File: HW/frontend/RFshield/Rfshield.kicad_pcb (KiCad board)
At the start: 4 copper layers, 73 x 50.9 mm, 270 parts, among them P10 TXENABLE, P11 RXENABLE, P12 XTAL2, P13 GCK1, P14 GCK2, P15 SGPIO_CLK, P16 DA0, P17 DA4, P18 DA7, P19 DD0, P2 VAA, P20 DD5, P21 DD9, P22 RSSI, P23 GND, P24 GND, P25 GND, P26 GND, P27 GND, P28 GND, P29 GND, P3 SCL, P30 GND, P31 GND, P32 GND, P33 XCVR_CLKOUT, P37 INTR, P38 CLKIN, P39 CLKOUT, P4 SDA, P5 SSP1_SCK, P6 SSP1_MOSI, P7 SSP1_MISO, P8 CS_XCVR, P9 CS_AD, Q1 MOSFET_P, T1 RX_BALUN, T2 TX_BALUN, U1 MAX2837, U2 MAX5864, U3 SI5351C, X1 GSG-XTAL4PIN

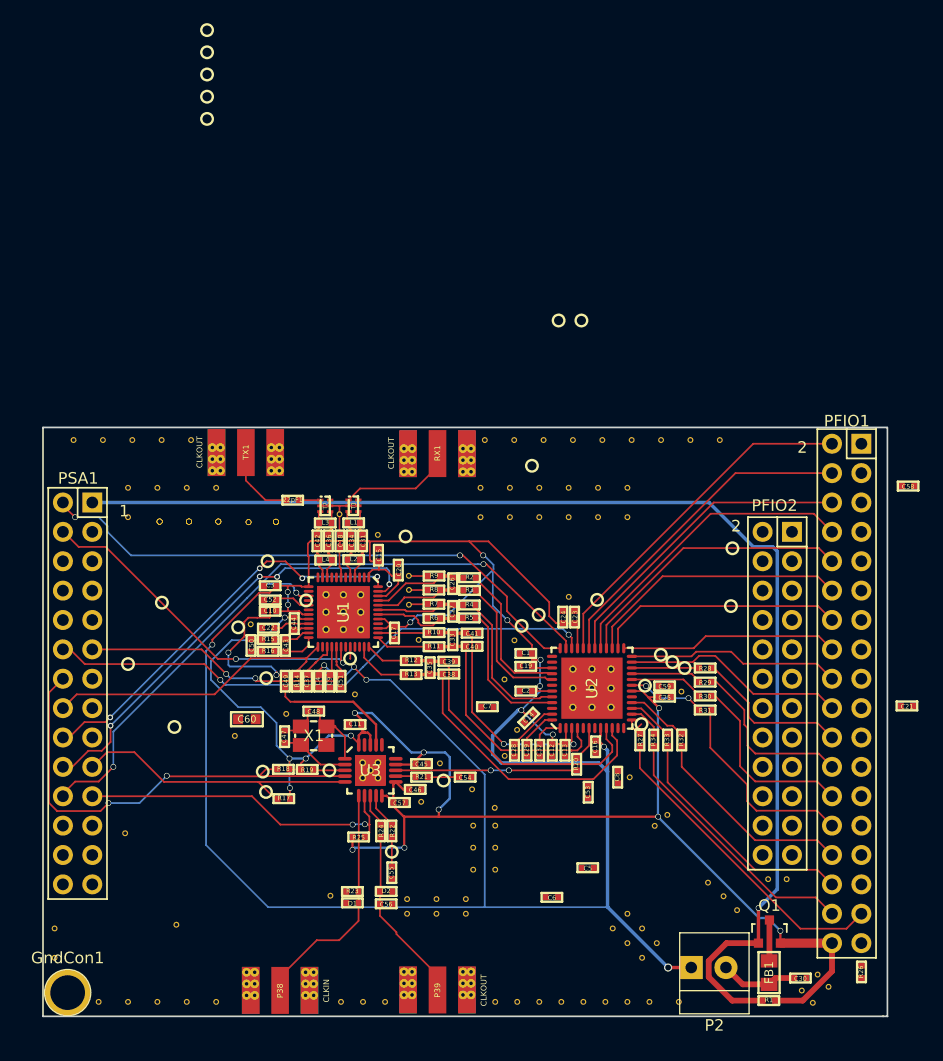
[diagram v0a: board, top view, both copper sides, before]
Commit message: pcb board has been finished
please check my pcb and spot the flaws
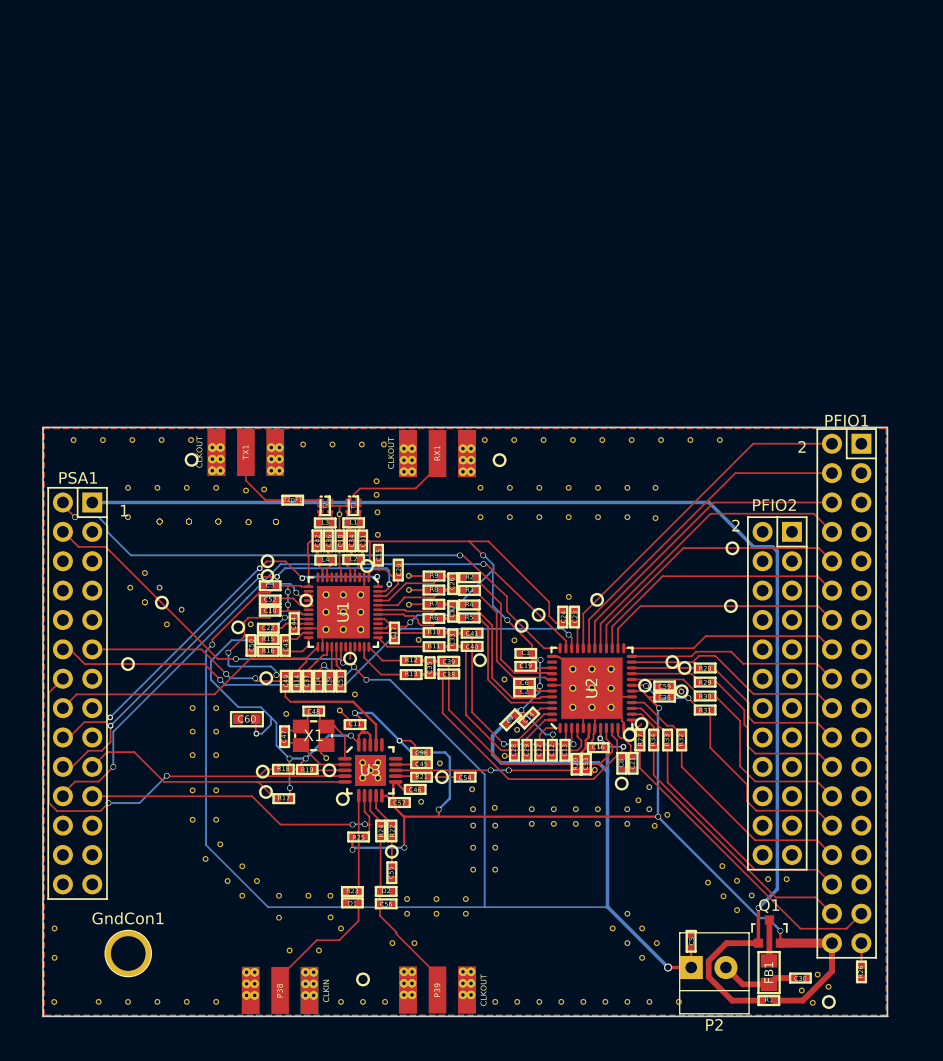
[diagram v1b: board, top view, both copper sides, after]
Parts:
- added TH13: CONN_1, opendous:1Pin_12mil_VIA, F.Cu at (34.3, 100.2)
- added TH13: CONN_1, opendous:1Pin_12mil_VIA, F.Cu at (32.2, 100.2)
- added TH13: CONN_1, opendous:1Pin_12mil_VIA, F.Cu at (34.3, 97.7)
- added TH13: CONN_1, opendous:1Pin_12mil_VIA, F.Cu at (32.2, 97.7)
- added TH13: CONN_1, opendous:1Pin_12mil_VIA, F.Cu at (32.2, 94.6)
- added TH13: CONN_1, opendous:1Pin_12mil_VIA, F.Cu at (34.3, 94.6)
- added TH13: CONN_1, opendous:1Pin_12mil_VIA, F.Cu at (34.3, 92.6)
- added TH13: CONN_1, opendous:1Pin_12mil_VIA, F.Cu at (32.2, 92.6)
- added TH151: CONN_1, opendous:1Pin_12mil_VIA, F.Cu at (72.3, 74.1)
- added TH151: CONN_1, opendous:1Pin_12mil_VIA, F.Cu at (72.3, 71.5)
- added TH18: CONN_1, opendous:1Pin_12mil_VIA, F.Cu at (67.0, 95.9)
- added TH18: CONN_1, opendous:1Pin_12mil_VIA, F.Cu at (42.3, 106.8)
- added TH18: CONN_1, opendous:1Pin_12mil_VIA, F.Cu at (56.5, 99.3)
- added TH18: CONN_1, opendous:1Pin_12mil_VIA, F.Cu at (61.6, 100.6)
- added TH18: CONN_1, opendous:1Pin_12mil_VIA, F.Cu at (61.6, 99.3)
- added TH18: CONN_1, opendous:1Pin_12mil_VIA, F.Cu at (63.5, 100.6)
- added TH18: CONN_1, opendous:1Pin_12mil_VIA, F.Cu at (63.5, 99.3)
- added TH18: CONN_1, opendous:1Pin_12mil_VIA, F.Cu at (65.4, 100.6)
- added TH18: CONN_1, opendous:1Pin_12mil_VIA, F.Cu at (65.4, 99.3)
- added TH18: CONN_1, opendous:1Pin_12mil_VIA, F.Cu at (67.3, 100.6)
- added TH18: CONN_1, opendous:1Pin_12mil_VIA, F.Cu at (69.8, 100.6)
- added TH18: CONN_1, opendous:1Pin_12mil_VIA, F.Cu at (33.4, 103.6)
- added TH18: CONN_1, opendous:1Pin_12mil_VIA, F.Cu at (67.3, 99.3)
- added TH18: CONN_1, opendous:1Pin_12mil_VIA, F.Cu at (69.8, 99.3)
- added TH18: CONN_1, opendous:1Pin_12mil_VIA, F.Cu at (71.7, 97.4)
- added TH18: CONN_1, opendous:1Pin_12mil_VIA, F.Cu at (71.7, 99.3)
- added TH18: CONN_1, opendous:1Pin_12mil_VIA, F.Cu at (78.0, 104.2)
- added TH18: CONN_1, opendous:1Pin_12mil_VIA, F.Cu at (79.3, 105.5)
- added TH18: CONN_1, opendous:1Pin_12mil_VIA, F.Cu at (80.6, 106.8)
- added TH18: CONN_1, opendous:1Pin_12mil_VIA, F.Cu at (34.6, 102.3)
- added TH18: CONN_1, opendous:1Pin_12mil_VIA, F.Cu at (35.3, 105.5)
- added TH18: CONN_1, opendous:1Pin_12mil_VIA, F.Cu at (36.5, 104.2)
- added TH18: CONN_1, opendous:1Pin_12mil_VIA, F.Cu at (36.5, 106.8)
- added TH18: CONN_1, opendous:1Pin_12mil_VIA, F.Cu at (37.8, 105.5)
- added TH18: CONN_1, opendous:1Pin_12mil_VIA, F.Cu at (39.7, 108.7)
- added TH18: CONN_1, opendous:1Pin_12mil_VIA, F.Cu at (39.7, 106.8)
- added TH23: CONN_1, opendous:1Pin_12mil_VIA, F.Cu at (46.9, 67.8)
- added TH23: CONN_1, opendous:1Pin_12mil_VIA, F.Cu at (44.3, 67.8)
- added TH23: CONN_1, opendous:1Pin_12mil_VIA, F.Cu at (41.8, 67.8)
- added TH23: CONN_1, opendous:1Pin_12mil_VIA, F.Cu at (48.8, 67.8)
- added TH23: CONN_1, opendous:1Pin_12mil_VIA, F.Cu at (48.1, 71.0)
- added TH23: CONN_1, opendous:1Pin_12mil_VIA, F.Cu at (48.1, 72.1)
- added TH23: CONN_1, opendous:1Pin_12mil_VIA, F.Cu at (48.2, 73.6)
- added TH25: CONN_1, opendous:1Pin_12mil_VIA, F.Cu at (45.0, 90.8)
- added TH28: CONN_1, opendous:1Pin_12mil_VIA, F.Cu at (30.0, 83.3)
- added TH28 (x2): CONN_1, opendous:1Pin_12mil_VIA, F.Cu at (28.1, 81.4)
- added TH28: CONN_1, opendous:1Pin_12mil_VIA, F.Cu at (31.3, 82.1)
- added TH28: CONN_1, opendous:1Pin_12mil_VIA, F.Cu at (29.4, 80.2)
- added TH28: CONN_1, opendous:1Pin_12mil_VIA, F.Cu at (26.9, 80.2)
- added TH28: CONN_1, opendous:1Pin_12mil_VIA, F.Cu at (28.1, 78.9)
- added TH30: CONN_1, opendous:1Pin_12mil_VIA, F.Cu at (38.4, 71.7)
- added TH30: CONN_1, opendous:1Pin_12mil_VIA, F.Cu at (36.9, 71.8)
- added TH34: CONN_1, opendous:1Pin_12mil_VIA, F.Cu at (45.1, 109.6)
- added TH34: CONN_1, opendous:1Pin_12mil_VIA, F.Cu at (40.6, 111.5)
- added TH34: CONN_1, opendous:1Pin_12mil_VIA, F.Cu at (43.2, 111.5)
- added TH34: CONN_1, opendous:1Pin_12mil_VIA, F.Cu at (49.5, 110.9)
- added TH34: CONN_1, opendous:1Pin_12mil_VIA, F.Cu at (51.4, 110.9)
- added TH40: CONN_1, opendous:1Pin_12mil_VIA, F.Cu at (43.8, 94.9)
- added TH45: CONN_1, opendous:1Pin_12mil_VIA, F.Cu at (44.2, 108.7)
- moved P24 98.2 mm to (87.3, 116.0)
- moved P28 67.8 mm to (70.0, 92.9)
- moved P23 67.5 mm to (45.2, 98.4)
- moved C58 48.0 mm to (52.0, 94.4)
- moved P31 41.1 mm to (47.3, 78.3)
- moved P27 40.2 mm to (69.3, 97.1)
- moved P32 31.4 mm to (32.2, 69.1)
- moved P25 30.1 mm to (57.1, 86.4)
- moved P29 27.3 mm to (47.0, 114.0)
- moved C21 24.2 mm to (70.3, 95.3), turned to 270 degrees
- moved C6 18.7 mm to (60.9, 88.4), turned to 180 degrees
- moved TH45 12.5 mm to (20.3, 116.0)
- moved P10 12.4 mm to (38.7, 79.1)
- moved TH13 12.3 mm to (32.2, 90.6)
- moved C5 11.0 mm to (75.3, 110.7), turned to 90 degrees
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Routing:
- net GND: track 15.4 -> 58.2 mm
- net VAA: track 239.3 -> 253.4 mm, vias 15 -> 16
- net VCC: track 140.9 -> 146.4 mm, vias 13 -> 14
- net Net-(PFIO1-Pad35): track 0.00 -> 1.96 mm
- net GCK1: track 3.04 -> 3.63 mm
- added copper zone on B.Cu, net GND
- added copper zone on F.Cu, net GND

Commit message: board finished after drc check
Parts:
- removed the TH13 at (34.3, 97.7)
- removed the TH13 at (32.2, 97.7)
- removed the TH30 at (34.3, 71.5)
- moved TH34 1.72 mm to (41.8, 110.3)
- moved TH34 0.47 mm to (51.9, 110.8)
- moved TH18 0.22 mm to (86.3, 113.4)
- moved C8 0.20 mm to (69.6, 95.3)
- moved TH18 0.13 mm to (84.8, 114.9)
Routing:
- net GND: track 58.2 -> 218.8 mm

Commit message: applying rf layout advice from maxim
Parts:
- added TH1: CONN_1, opendous:1Pin_12mil_VIA, F.Cu at (52.7, 98.3)
- added TH26: CONN_1, opendous:1Pin_12mil_VIA, F.Cu at (37.4, 82.1)
- added TH41: CONN_1, opendous:1Pin_12mil_VIA, F.Cu at (51.7, 82.8)
- added TH41: CONN_1, opendous:1Pin_12mil_VIA, F.Cu at (55.1, 88.6)
- added TH41: CONN_1, opendous:1Pin_12mil_VIA, F.Cu at (57.1, 87.4)
- moved P29 1.92 mm to (47.0, 116.0)
- moved TH1 0.91 mm to (51.4, 99.3)
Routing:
- net GND: track 218.8 -> 241.3 mm
- net VAA: track 253.2 -> 249.5 mm
- net /TXBBI-: track 8.49 -> 8.43 mm, vias 0 -> 2
